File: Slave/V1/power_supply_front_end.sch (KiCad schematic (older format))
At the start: 16 parts, among them U202 AP3015KTR-G1, U203 AP2202K-ADJTRG1

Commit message: clear annotation
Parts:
- renumbered C201 to C?, C202 to C?, C205 to C?, C204 to C?, C203 to C?, D201 to D?, L202 to L?, L201 to L?, R203 to R?, R205 to R?, R202 to R?, R204 to R?, R207 to R?, U202 to U?, U203 to U?
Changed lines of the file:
@@
 $EndDescr
 $Comp
-L AP3015KTR-G1 U202
+L AP3015KTR-G1 U?
 U 1 1 591B2FEB
 P 4900 2900
-F 0 "U202" H 4900 3220 60  0000 C CNN
+F 0 "U?" H 4900 3220 60  0000 C CNN
 F 1 "AP3015KTR-G1" H 4900 2560 60  0000 C CNN
 F 2 "IC:SOT-23-5" H 4900 475 60  0001 C CNN
@@
 $EndComp
 $Comp
-L AP2202K-ADJTRG1 U203
+L AP2202K-ADJTRG1 U?
 U 1 1 591B30B0
 P 4500 5000
-F 0 "U203" H 4500 5300 60  0000 C CNN
+F 0 "U?" H 4500 5300 60  0000 C CNN
 F 1 "AP2202K-ADJTRG1" H 4500 4660 60  0000 C CNN
 F 2 "IC:SOT-23-5" H 4500 3395 60  0001 C CNN
@@
 $EndComp
 $Comp
-L LQM31PN4R7M00L L202
+L LQM31PN4R7M00L L?
 U 1 1 591BB94D
 P 4900 2200
-F 0 "L202" H 4890 2360 60  0000 C CNN
+F 0 "L?" H 4890 2360 60  0000 C CNN
 F 1 "LQM31PN4R7M00L" H 4900 1900 60  0001 C CNN
 F 2 "Inductors:I1206" H 4900 1300 60  0001 C CNN
@@
 $EndComp
 $Comp
-L LBC3225T101KR L201
+L LBC3225T101KR L?
 U 1 1 591BBA8F
 P 4900 1800
-F 0 "L201" H 4900 1900 60  0000 C CNN
+F 0 "L?" H 4900 1900 60  0000 C CNN
 F 1 "LBC3225T101KR" H 4900 1450 60  0001 C CNN
 F 2 "Inductors:LBC3225" H 4900 850 60  0001 C CNN
@@
 ONLY SOLDER ONE
 $Comp
-L 885012107014 C201
+L 885012107014 C?
 U 1 1 591BCA3D
 P 3900 2100
-F 0 "C201" H 3850 2260 60  0000 C CNN
+F 0 "C?" H 3850 2260 60  0000 C CNN
 F 1 "885012107014" H 3850 1750 60  0001 C CNN
 F 2 "Capacitors:C0805" H 3850 1150 60  0001 C CNN
@@
 $EndComp
 $Comp
-L BGND #PWR022
+L BGND #PWR?
 U 1 1 591BCD04
 P 3900 2500
-F 0 "#PWR022" H 3900 2330 50  0001 C CNN
+F 0 "#PWR?" H 3900 2330 50  0001 C CNN
 F 1 "BGND" H 3900 2400 50  0000 C CNN
 F 2 "" H 3900 2600 60  0000 C CNN
@@
 $EndComp
 $Comp
-L RC0805JR-07470KL R203
+L RC0805JR-07470KL R?
 U 1 1 591BCFD2
 P 3600 3200
-F 0 "R203" H 3600 3280 60  0000 C CNN
+F 0 "R?" H 3600 3280 60  0000 C CNN
 F 1 "RC0805JR-07470KL" H 3600 2900 50  0001 C CNN
 F 2 "Resistors:R0805" H 3600 2300 30  0001 C CNN
@@
 $EndComp
 $Comp
-L NSR0530HT1G D201
+L NSR0530HT1G D?
 U 1 1 591BD4B8
 P 5700 1800
-F 0 "D201" H 5600 2100 60  0000 C CNN
+F 0 "D?" H 5600 2100 60  0000 C CNN
 F 1 "NSR0530HT1G" H 5800 2000 60  0000 C CNN
 F 2 "Diodes:SOD-323" H 5680 800 60  0001 C CNN
@@
 $EndComp
 $Comp
-L 885012107014 C202
+L 885012107014 C?
 U 1 1 591BE5E6
 P 6300 2400
-F 0 "C202" H 6250 2560 60  0000 C CNN
+F 0 "C?" H 6250 2560 60  0000 C CNN
 F 1 "885012107014" H 6250 2050 60  0001 C CNN
 F 2 "Capacitors:C0805" H 6250 1450 60  0001 C CNN
@@
 $EndComp
 $Comp
-L BGND #PWR024
+L BGND #PWR?
 U 1 1 591BE78A
 P 6300 2800
-F 0 "#PWR024" H 6300 2630 50  0001 C CNN
+F 0 "#PWR?" H 6300 2630 50  0001 C CNN
 F 1 "BGND" H 6300 2700 50  0000 C CNN
 F 2 "" H 6300 2900 60  0000 C CNN
@@
 $EndComp
 $Comp
-L 885012107014 C205
+L 885012107014 C?
 U 1 1 591BED58
 P 3500 5100
-F 0 "C205" H 3450 5260 60  0000 C CNN
+F 0 "C?" H 3450 5260 60  0000 C CNN
 F 1 "885012107014" H 3450 4750 60  0001 C CNN
 F 2 "Capacitors:C0805" H 3450 4150 60  0001 C CNN
@@
 $EndComp
 $Comp
-L RC0805JR-0710KL R205
+L RC0805JR-0710KL R?
 U 1 1 591BF403
 P 3900 5000
-F 0 "R205" H 3900 5080 60  0000 C CNN
+F 0 "R?" H 3900 5080 60  0000 C CNN
 F 1 "RC0805JR-0710KL" H 3900 4700 50  0001 C CNN
 F 2 "Resistors:R0805" H 3900 4100 30  0001 C CNN
@@
 $EndComp
 $Comp
-L 885012107014 C204
+L 885012107014 C?
 U 1 1 591BF617
 P 6200 5000
-F 0 "C204" H 6150 5160 60  0000 C CNN
+F 0 "C?" H 6150 5160 60  0000 C CNN
 F 1 "885012107014" H 6150 4650 60  0001 C CNN
 F 2 "Capacitors:C0805" H 6150 4050 60  0001 C CNN
@@
 $EndComp
 $Comp
-L 885012107014 C203
+L 885012107014 C?
 U 1 1 591BFD48
 P 6800 2400
-F 0 "C203" H 6750 2560 60  0000 C CNN
+F 0 "C?" H 6750 2560 60  0000 C CNN
 F 1 "885012107014" H 6750 2050 60  0001 C CNN
 F 2 "Capacitors:C0805" H 6750 1450 60  0001 C CNN
@@
 $EndComp
 $Comp
-L BGND #PWR028
+L BGND #PWR?
 U 1 1 591C023A
 P 6800 2800
-F 0 "#PWR028" H 6800 2630 50  0001 C CNN
+F 0 "#PWR?" H 6800 2630 50  0001 C CNN
 F 1 "BGND" H 6800 2700 50  0000 C CNN
 F 2 "" H 6800 2900 60  0000 C CNN
@@
 $EndComp
 $Comp
-L RC0805JR-071ML R202
+L RC0805JR-071ML R?
 U 1 1 591C2F0F
 P 5900 2600
-F 0 "R202" H 5900 2680 60  0000 C CNN
+F 0 "R?" H 5900 2680 60  0000 C CNN
 F 1 "RC0805JR-071ML" H 5900 2300 50  0001 C CNN
 F 2 "Resistors:R0805" H 5900 1700 30  0001 C CNN
@@
 $EndComp
 $Comp
-L RC0805FR-07324KL R204
+L RC0805FR-07324KL R?
 U 1 1 591C3C0D
 P 5900 3200
-F 0 "R204" H 5900 3280 60  0000 C CNN
+F 0 "R?" H 5900 3280 60  0000 C CNN
 F 1 "RC0805FR-07324KL" H 5900 2900 50  0001 C CNN
 F 2 "Resistors:R0805" H 5900 2300 30  0001 C CNN
@@
 $EndComp
 $Comp
-L RT0805BRD0712K7L R207
+L RT0805BRD0712K7L R?
 U 1 1 591C47EB
 P 5200 5800
-F 0 "R207" H 5200 5880 60  0000 C CNN
+F 0 "R?" H 5200 5880 60  0000 C CNN
 F 1 "RT0805BRD0712K7L" H 5200 5500 50  0001 C CNN
 F 2 "Resistors:R0805" H 5200 4900 30  0001 C CNN

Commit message: placing components
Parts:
- removed L?: LQM31PN4R7M00L, Inductors:I1206, symbol LQM31PN4R7M00L
- removed L?: LBC3225T101KR, Inductors:LBC3225, symbol LBC3225T101KR
- removed R?: RC0805JR-07470KL, Resistors:R0805, symbol RC0805JR-07470KL
- removed R?: RC0805JR-0710KL, Resistors:R0805, symbol RC0805JR-0710KL
- removed R?: RT0805BRD0712K7L, Resistors:R0805, symbol RT0805BRD0712K7L
- added L601: MLZ2012N101LT000, Inductors:I0805, symbol MLZ2012N101LT000
- added R604: RC0805FR-0712K1L, Resistors:R0805, symbol RC0805FR-0712K1L
- gave numbers to parts that had none: 11
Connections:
- wire segments 46 -> 42
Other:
- note removed: "ONLY SOLDER ONE"

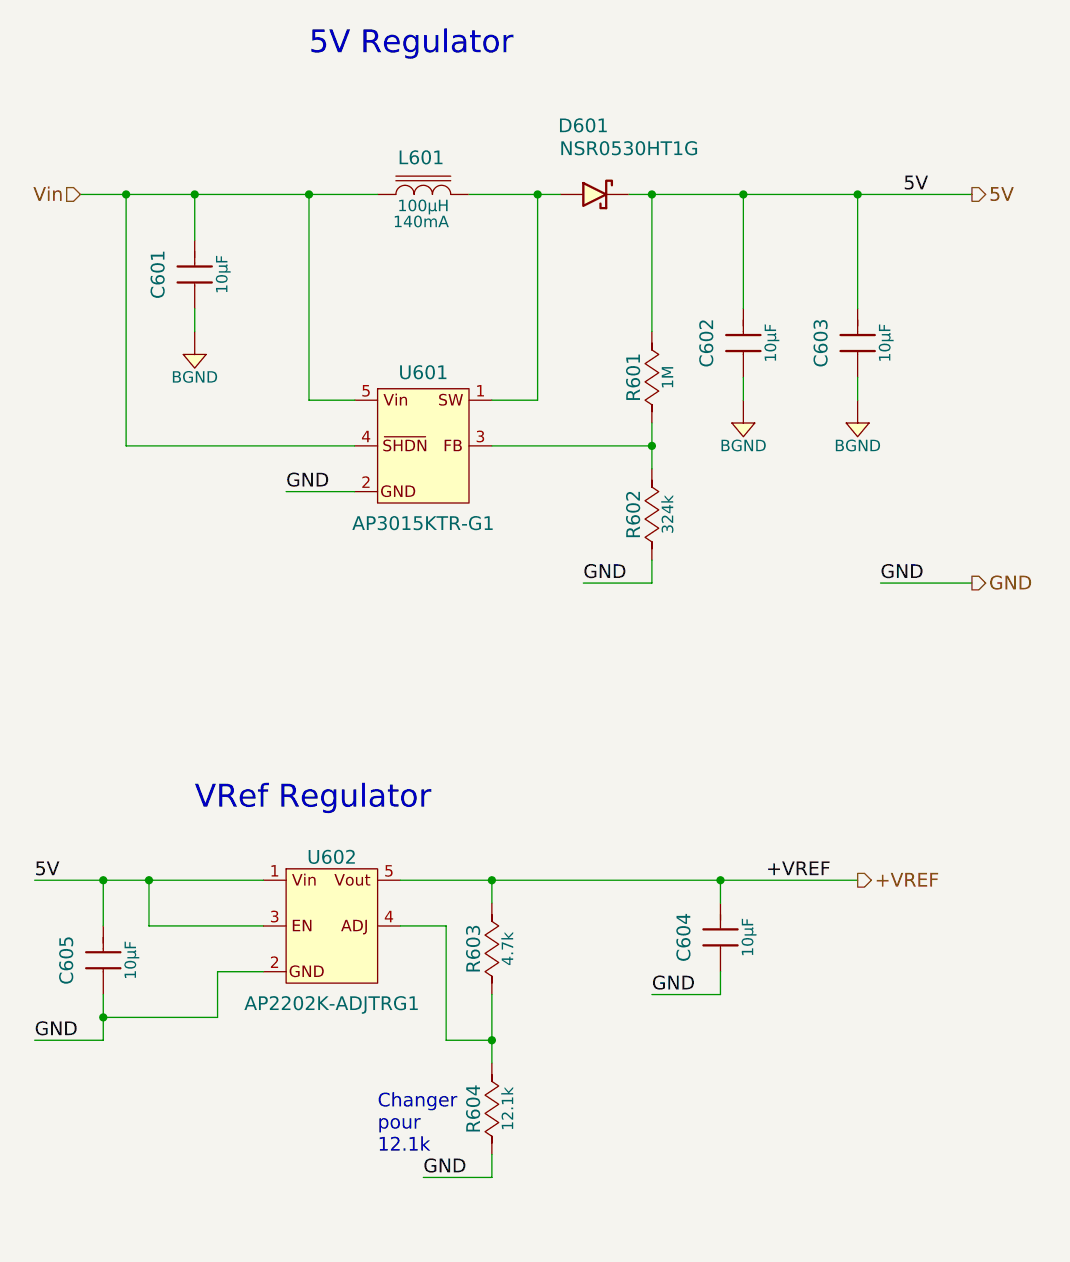
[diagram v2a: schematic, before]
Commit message: placing component on front end
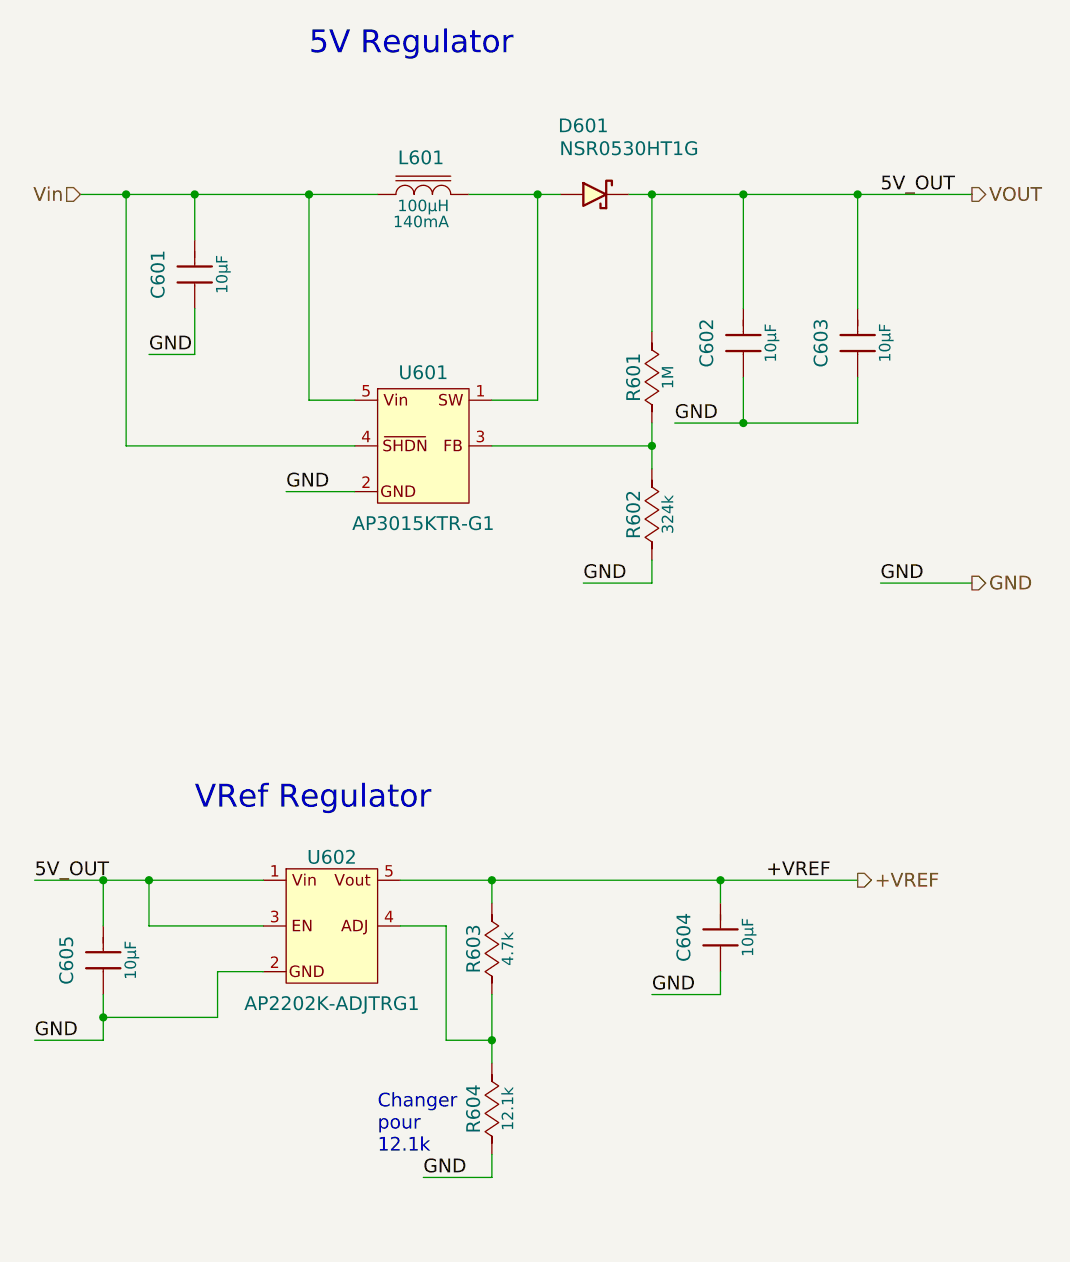
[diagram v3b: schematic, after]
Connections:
- net BGND is gone; now on net GND: C601.1, C602.1, C603.1
- net 5V renamed VOUT
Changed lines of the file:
@@
-$EndComp
-$Comp
-L BGND #PWR060
-U 1 1 591BCD04
-P 3900 2500
-F 0 "#PWR060" H 3900 2330 50  0001 C CNN
-F 1 "BGND" H 3900 2400 50  0000 C CNN
-F 2 "" H 3900 2600 60  0000 C CNN
-F 3 "" H 3880 2410 60  0000 C CNN
-	1    3900 2500
-	1    0    0    -1
 $EndComp
 $Comp
@@
 $EndComp
 $Comp
-L BGND #PWR061
-U 1 1 591BE78A
-P 6300 2800
-F 0 "#PWR061" H 6300 2630 50  0001 C CNN
-F 1 "BGND" H 6300 2700 50  0000 C CNN
-F 2 "" H 6300 2900 60  0000 C CNN
-F 3 "" H 6280 2710 60  0000 C CNN
-	1    6300 2800
-	1    0    0    -1
-$EndComp
-$Comp
 L 885012107014 C605
 U 1 1 591BED58
@@
 $EndComp
 $Comp
-L BGND #PWR062
-U 1 1 591C023A
-P 6800 2800
-F 0 "#PWR062" H 6800 2630 50  0001 C CNN
-F 1 "BGND" H 6800 2700 50  0000 C CNN
-F 2 "" H 6800 2900 60  0000 C CNN
-F 3 "" H 6780 2710 60  0000 C CNN
-	1    6800 2800
-	1    0    0    -1
-$EndComp
-$Comp
 L RC0805JR-071ML R601
 U 1 1 591C2F0F
@@
 Connection ~ 4400 1800
 Wire Wire Line
-	3900 2300 3900 2400
+	3900 2300 3900 2500
 Wire Wire Line
 	3900 2000 3900 1800
@@
 Connection ~ 6300 1800
 Wire Wire Line
-	6300 2600 6300 2700
+	6300 2600 6300 2800
 Wire Wire Line
 	3200 4800 4200 4800
@@
 Connection ~ 6800 1800
 Wire Wire Line
-	6800 2600 6800 2700
+	6800 2800 6800 2600
 Wire Wire Line
 	5900 2400 5900 1800
@@
 	0    -1   -1   0
 $EndComp
-Text Label 7000 1800 0    60   ~ 0
-5V
+Text Label 6900 1800 0    60   ~ 0
+5V_OUT
 Text Label 6400 4800 0    60   ~ 0
 +VREF
 Text Label 3200 4800 0    60   ~ 0
-5V
+5V_OUT
 Text HLabel 7300 1800 2    60   Output ~ 0
-5V
+VOUT
 Text HLabel 6800 4800 2    60   Output ~ 0
 +VREF
@@
 	1    0    0    -1
 $EndComp
+Text Label 6000 2800 0    60   ~ 0
+GND
+Wire Wire Line
+	6000 2800 6800 2800
+Connection ~ 6300 2800
+Wire Wire Line
+	3900 2500 3700 2500
+Text Label 3700 2500 0    60   ~ 0
+GND
 $EndSCHEMATC
